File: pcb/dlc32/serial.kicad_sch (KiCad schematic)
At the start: 18 parts, among them IC4 AMS1117-3.3, J10 TO_J7, J11 24V PWR, J12 LED LIGHTING, J13 AIR VALVE, J14 AIMING LASER, J15 CHILLER POWER, J16 CHILLER SSR, J5 POWEROFF, Q1 ZXMN4A06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

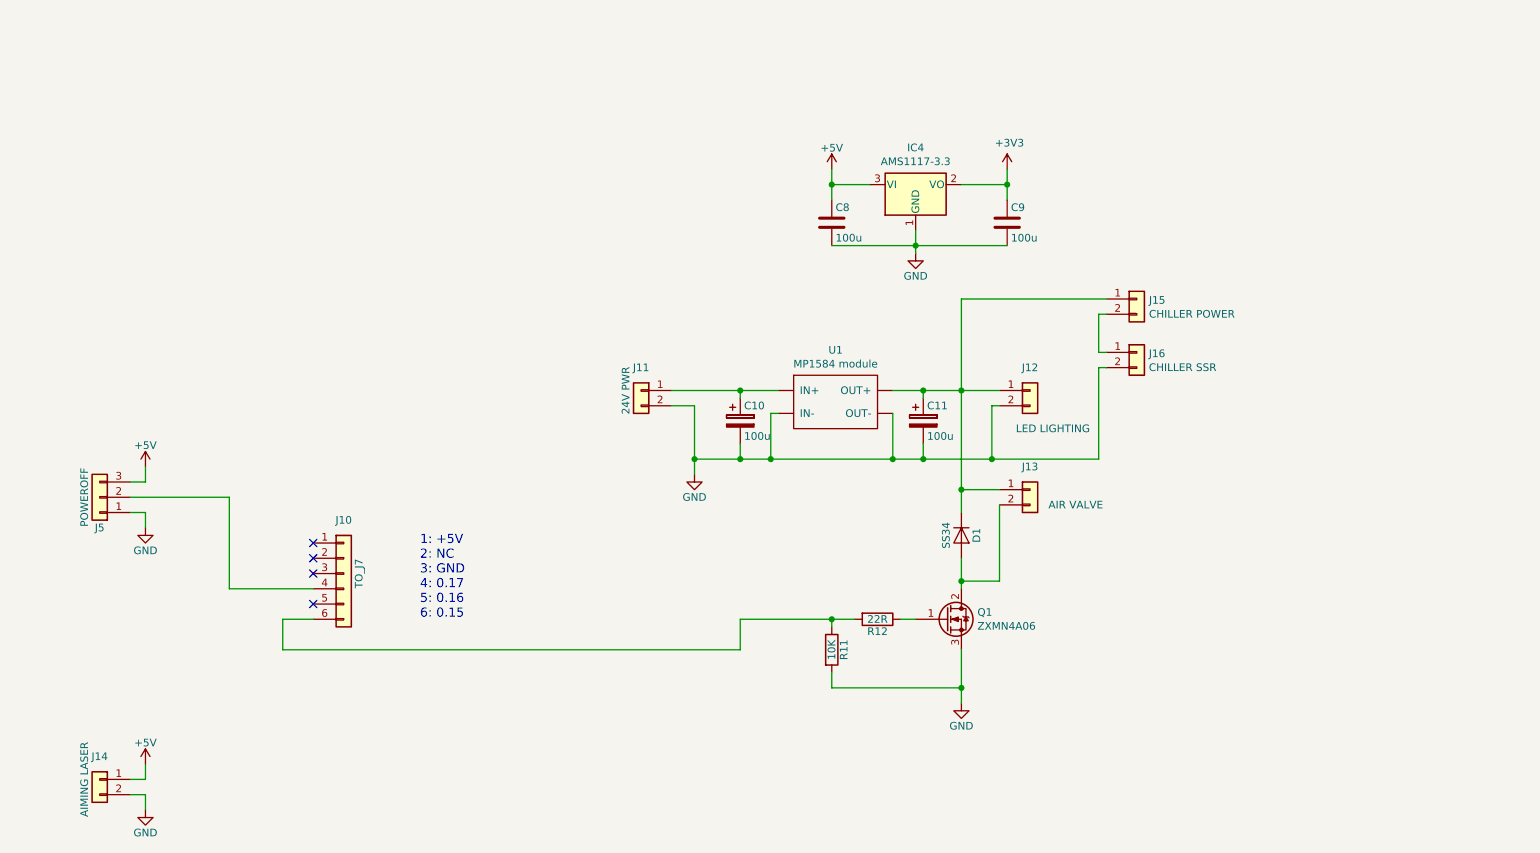
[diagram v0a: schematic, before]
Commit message: Update symbols etc, remove obsolete parts.
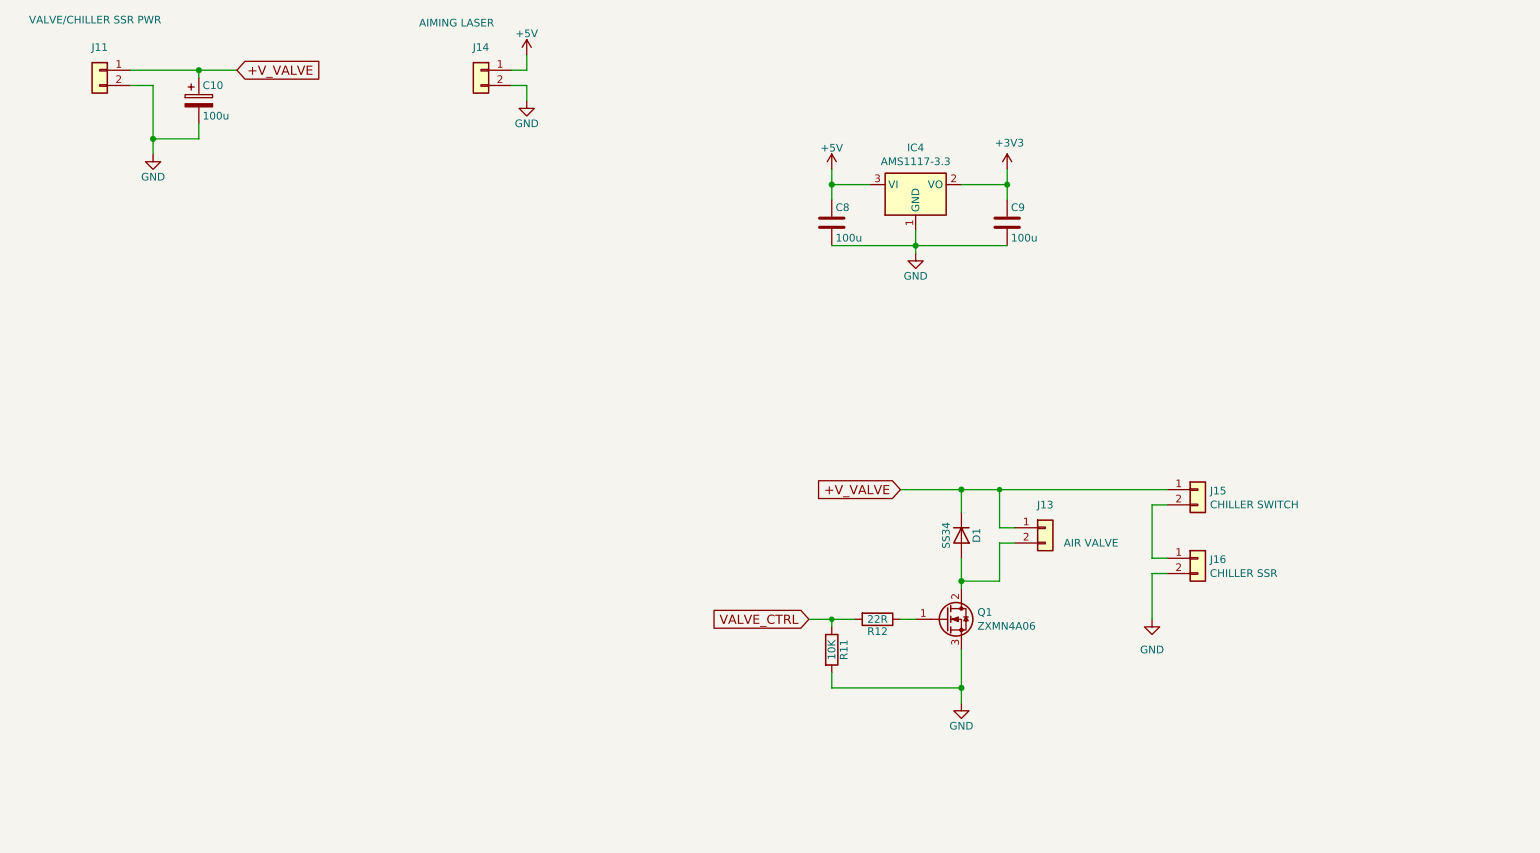
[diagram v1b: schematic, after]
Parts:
- removed C11: 100u, Capacitor_SMD:CP_Elec_10x10, symbol Device:CP
- removed J10: TO_J7, Connector_JST:JST_XH_B06B-XH-A_1x06_P2.50mm_Vertical, symbol Connector_Generic:Conn_01x06
- removed J12: LED LIGHTING, Connector_JST:JST_PH_B2B-PH-K_1x02_P2.00mm_Vertical, symbol Connector_Generic:Conn_01x02
- removed J5: POWEROFF, Connector_JST:JST_PH_B3B-PH-K_1x03_P2.00mm_Vertical, symbol Connector_Generic:Conn_01x03
- removed U1: MP1584 module, dlc32:MP1584-module, symbol buck-converter:buck-converter
- C10: symbol Device:CP -> Device:C_Polarized
- J11: value 24V PWR -> VALVE/CHILLER SSR PWR
- J15: value CHILLER POWER -> CHILLER SWITCH
- Q1: symbol Device:Q_NMOS_GDS -> Transistor_FET:Q_NMOS_GDS
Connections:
- net VALVE_CTRL: now reaches R11.1, R12.2
- net +V_VALVE: now reaches C10.1, J11.1 (Pin_1)
- net +V_VALVE: now also D1.1 (K), J13.1 (Pin_1), J15.1 (Pin_1)
- no-connect marks 4 -> 0
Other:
- note removed: "1: +5V 2: NC 3: GND 4: 0.17 5: 0.16 6: 0.15"
- moved on the sheet: J11, J13, J14, J15, J16

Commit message: Renumber, delete PCB.
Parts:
- C8, C9: value 100u -> 22u; footprint Capacitor_SMD:CP_Elec_10x10 -> (none)
- renumbered C10 to C6, J11 to J10, J15 to J4, J16 to J5, J13 to J6, J14 to J9
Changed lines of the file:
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@@
 			)
 		)
-		(property "Value" "100u"
+		(property "Value" "22u"
 			(at 160.655 63.5 0)
 			(effects
@@
 			)
 		)
-		(property "Footprint" "Capacitor_SMD:CP_Elec_10x10"
+		(property "Footprint" ""
 			(at 160.9852 64.77 0)
 			(effects
@@
 			)
 		)
-		(property "Value" "100u"
+		(property "Value" "22u"
 			(at 189.865 63.5 0)
 			(effects
@@
 			)
 		)
-		(property "Footprint" "Capacitor_SMD:CP_Elec_10x10"
+		(property "Footprint" ""
 			(at 190.1952 64.77 0)
 			(effects
@@
 		(on_board yes)
 		(dnp no)
-		(property "Reference" "J14"
+		(property "Reference" "J9"
 			(at 101.6 31.75 0)
 			(effects
@@
 			(project ""
 				(path "/fc0b2ef6-7d8e-4322-8468-8fac0c3c3d07/00000000-0000-0000-0000-000058f3b713"
-					(reference "J14")
+					(reference "J9")
 					(unit 1)
 				)
@@
 		(on_board yes)
 		(dnp no)
-		(property "Reference" "J11"
+		(property "Reference" "J10"
 			(at 38.1 31.75 0)
 			(effects
@@
 			(project ""
 				(path "/fc0b2ef6-7d8e-4322-8468-8fac0c3c3d07/00000000-0000-0000-0000-000058f3b713"
-					(reference "J11")
+					(reference "J10")
 					(unit 1)
 				)
@@
 		(on_board yes)
 		(dnp no)
-		(property "Reference" "C10"
+		(property "Reference" "C6"
 			(at 55.245 38.1 0)
 			(effects
@@
 			(project ""
 				(path "/fc0b2ef6-7d8e-4322-8468-8fac0c3c3d07/00000000-0000-0000-0000-000058f3b713"
-					(reference "C10")
+					(reference "C6")
 					(unit 1)
 				)
@@
 		(on_board yes)
 		(dnp no)
-		(property "Reference" "J13"
+		(property "Reference" "J6"
 			(at 195.58 107.95 0)
 			(effects
@@
 			(project ""
 				(path "/fc0b2ef6-7d8e-4322-8468-8fac0c3c3d07/00000000-0000-0000-0000-000058f3b713"
-					(reference "J13")
+					(reference "J6")
 					(unit 1)
 				)
@@
 		(on_board yes)
 		(dnp no)
-		(property "Reference" "J15"
+		(property "Reference" "J4"
 			(at 223.012 105.6132 0)
 			(effects
@@
 			(project ""
 				(path "/fc0b2ef6-7d8e-4322-8468-8fac0c3c3d07/00000000-0000-0000-0000-000058f3b713"
-					(reference "J15")
+					(reference "J4")
 					(unit 1)
 				)
@@
 		(on_board yes)
 		(dnp no)
-		(property "Reference" "J16"
+		(property "Reference" "J5"
 			(at 222.9866 117.0432 0)
 			(effects
@@
 			(project ""
 				(path "/fc0b2ef6-7d8e-4322-8468-8fac0c3c3d07/00000000-0000-0000-0000-000058f3b713"
-					(reference "J16")
-					(unit 1)
-				)
+					(reference "J5")
+					(unit 1)
+				)

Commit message: Add block diagram.
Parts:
- C8, C9: footprint (none) -> Capacitor_Tantalum_SMD:CP_EIA-3528-21_Kemet-B
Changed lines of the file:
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@@
 			)
 		)
-		(property "Footprint" ""
+		(property "Footprint" "Capacitor_Tantalum_SMD:CP_EIA-3528-21_Kemet-B"
 			(at 160.9852 64.77 0)
 			(effects
@@
 			)
 		)
-		(property "Footprint" ""
+		(property "Footprint" "Capacitor_Tantalum_SMD:CP_EIA-3528-21_Kemet-B"
 			(at 190.1952 64.77 0)
 			(effects

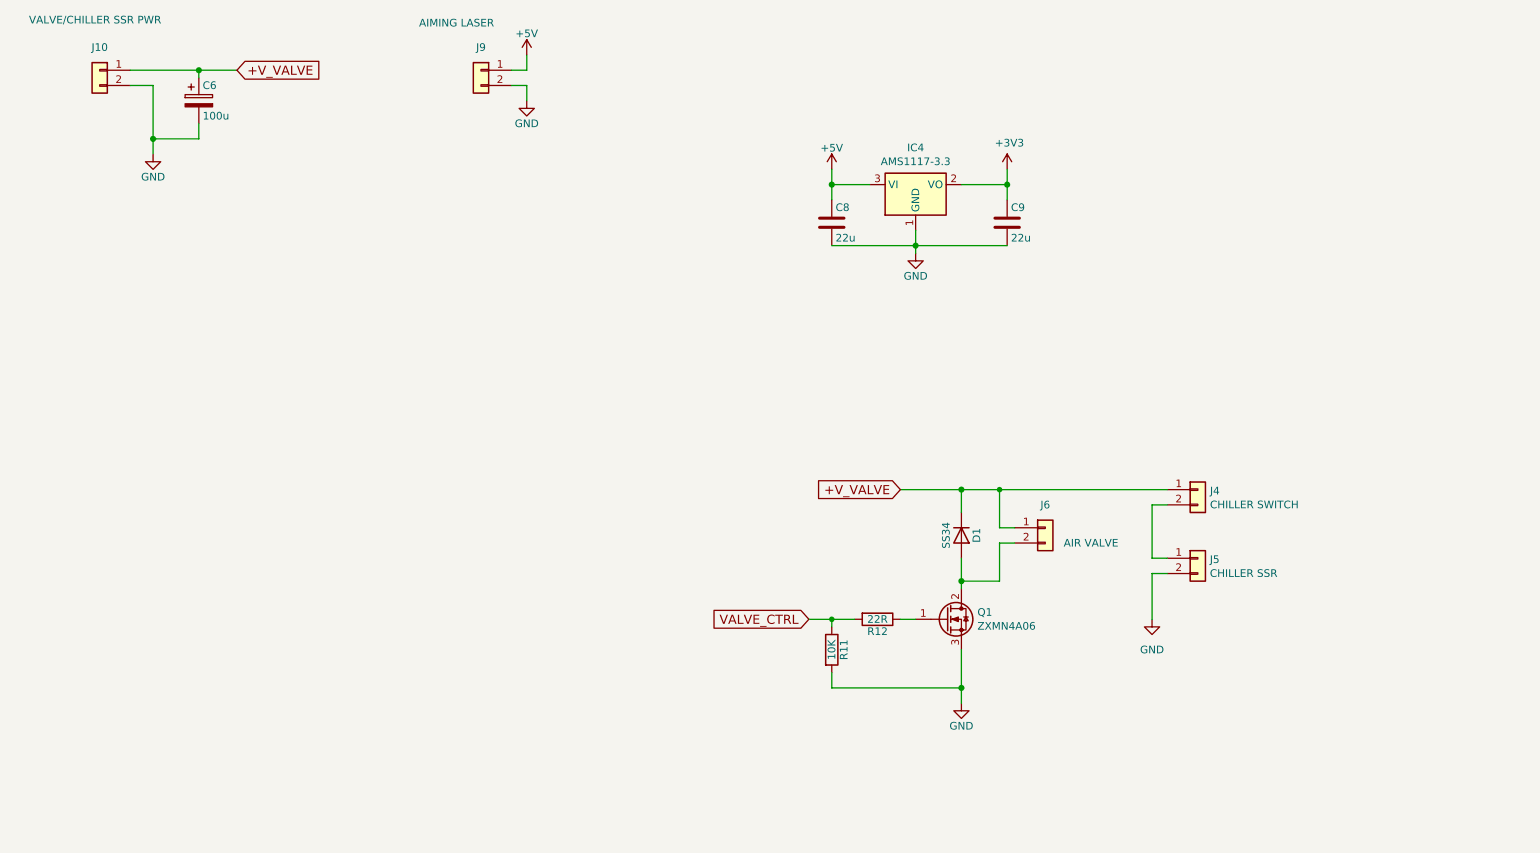
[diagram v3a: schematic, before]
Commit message: Include exhaust control in dlc32 pcb.
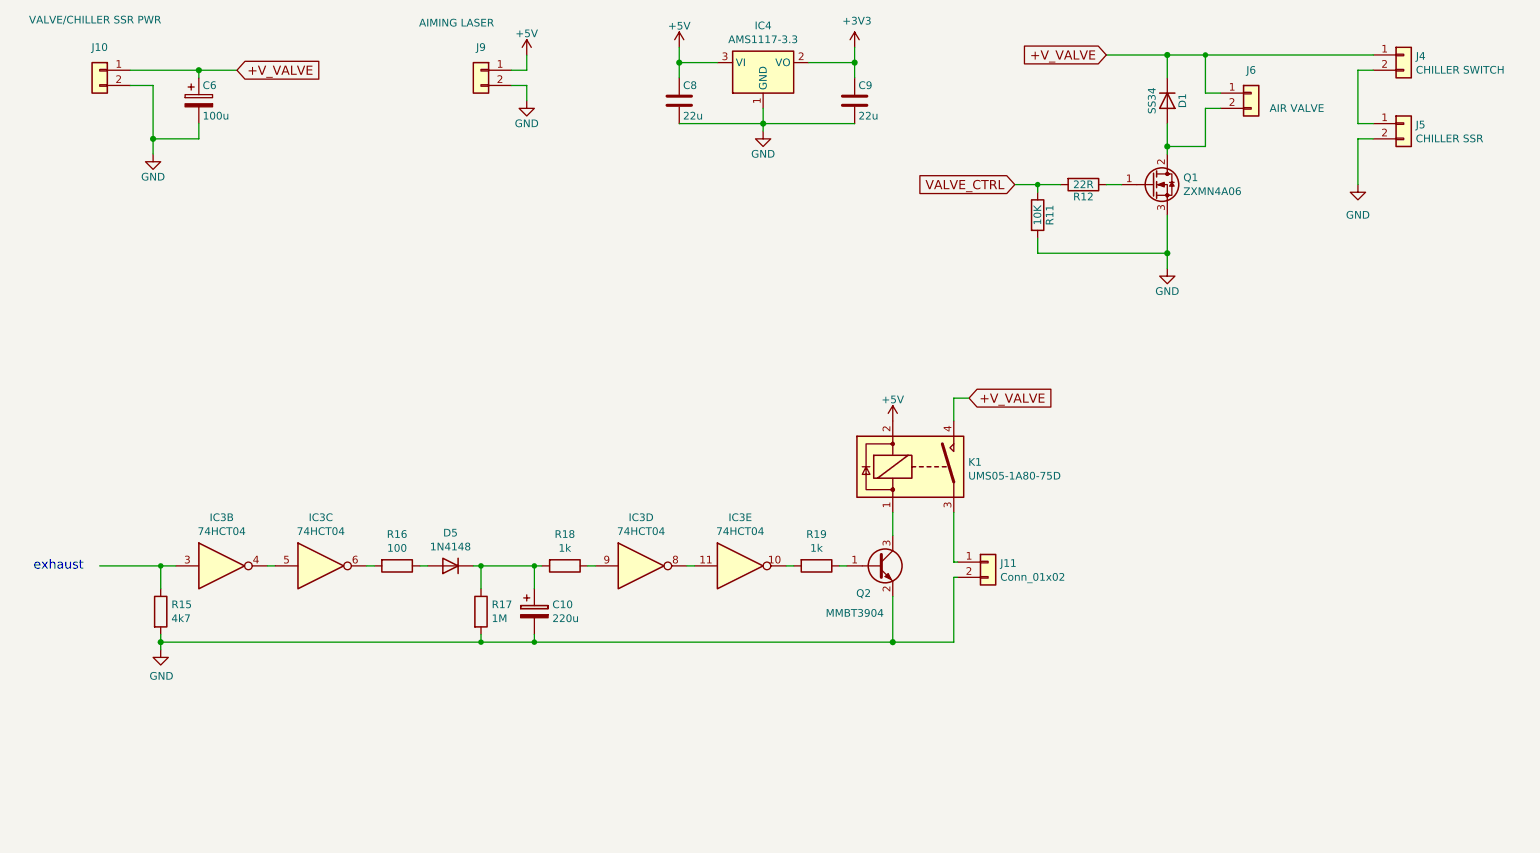
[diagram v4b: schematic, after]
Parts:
- added C10: 220u, Capacitor_SMD:CP_Elec_10x10, symbol Device:CP
- added D5: 1N4148, Diode_SMD:D_MiniMELF, symbol Device:D
- added IC3: 74HCT04, Package_SO:SOIC-14_3.9x8.7mm_P1.27mm, symbol 74xx:74HCT04
- added J11: Conn_01x02, Connector_JST:JST_XH_B02B-XH-A_1x02_P2.50mm_Vertical, symbol Connector_Generic:Conn_01x02
- added K1: UMS05-1A80-75D, Exhaustcontrol:DIL-relay, symbol ums05-1a80-75d:UMS05-1A80-75D
- added Q2: MMBT3904, Package_TO_SOT_SMD:SOT-23, symbol Transistor_BJT:MMBT3904
- added R15: 4k7, Resistor_SMD:R_0603_1608Metric, symbol Device:R
- added R16: 100, Resistor_SMD:R_0603_1608Metric, symbol Device:R
- added R17: 1M, Resistor_SMD:R_0603_1608Metric, symbol Device:R
- added R18, R19: 1k, Resistor_SMD:R_0603_1608Metric, symbol Device:R
- J10, J4, J5, J6, J9: footprint Connector_JST:JST_PH_B2B-PH-K_1x02_P2.00mm_Vertical -> Connector_JST:JST_XH_B2B-XH-A_1x02_P2.50mm_Vertical
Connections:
- net +5V: now also K1.2
- net +V_VALVE: now also K1.4
- net GND: now also C10.2, J11.2 (Pin_2), Q2.2 (E), R15.2, R17.2
- new net: IC3.11, IC3.8
- new net: IC3.9, R18.1
- new net: C10.1, D5.1 (K), R17.1, R18.2
- new net: IC3.3, R15.1
- new net: IC3.4, IC3.5
- new net: IC3.6, R16.2
- new net: K1.1, Q2.3 (C)
- new net: J11.1 (Pin_1), K1.3
- new net: Q2.1 (B), R19.1
- new net: IC3.10, R19.2
- new net: D5.2 (A), R16.1
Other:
- note added: "exhaust"
- moved on the sheet: C8, C9, D1, IC4, J4, J5, J6, Q1, R11, R12

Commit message: Simplify.
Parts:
- removed C8, C9: 22u, Capacitor_Tantalum_SMD:CP_EIA-3528-21_Kemet-B, symbol Device:C
- removed IC4: AMS1117-3.3, Package_TO_SOT_SMD:SOT-223-3_TabPin2, symbol Regulator_Linear:AMS1117-3.3
- renumbered C10 to C7, IC3 to IC2
